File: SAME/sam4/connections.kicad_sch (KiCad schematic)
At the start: 27 parts, among them J11 Conn_01x02_Socket, J13 BM04B-GHS-TBT, J14 BM04B-GHS-TBT, J15 BM04B-GHS-TBT, J16 BM04B-GHS-TBT, J17 BM04B-GHS-TBT, J18 5023860270, J19 BM04B-GHS-TBT, J6 XT60PW-M, J7 XT60PW-M, J8 XT30PW-F, J9 GT-USB-7010ASV, M5 MR30PW-FB

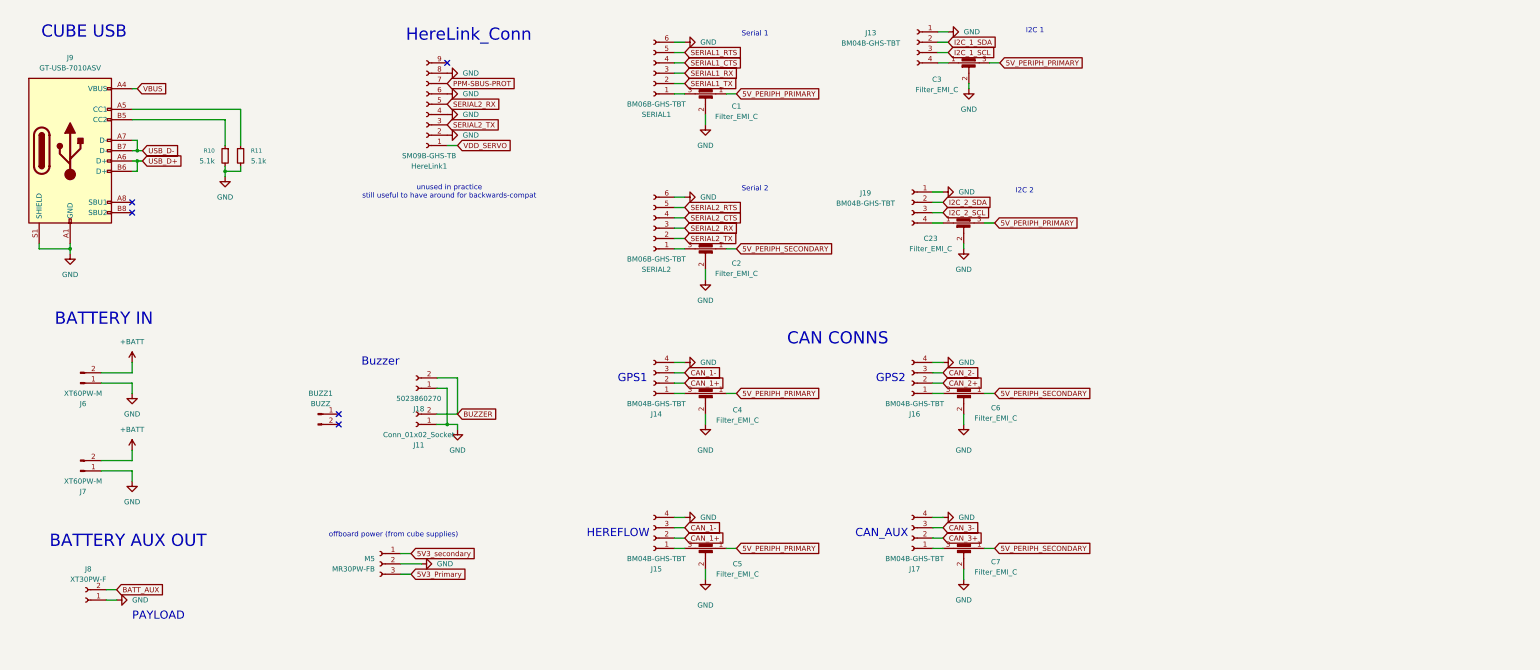
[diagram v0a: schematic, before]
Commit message: final san check routing. add protection
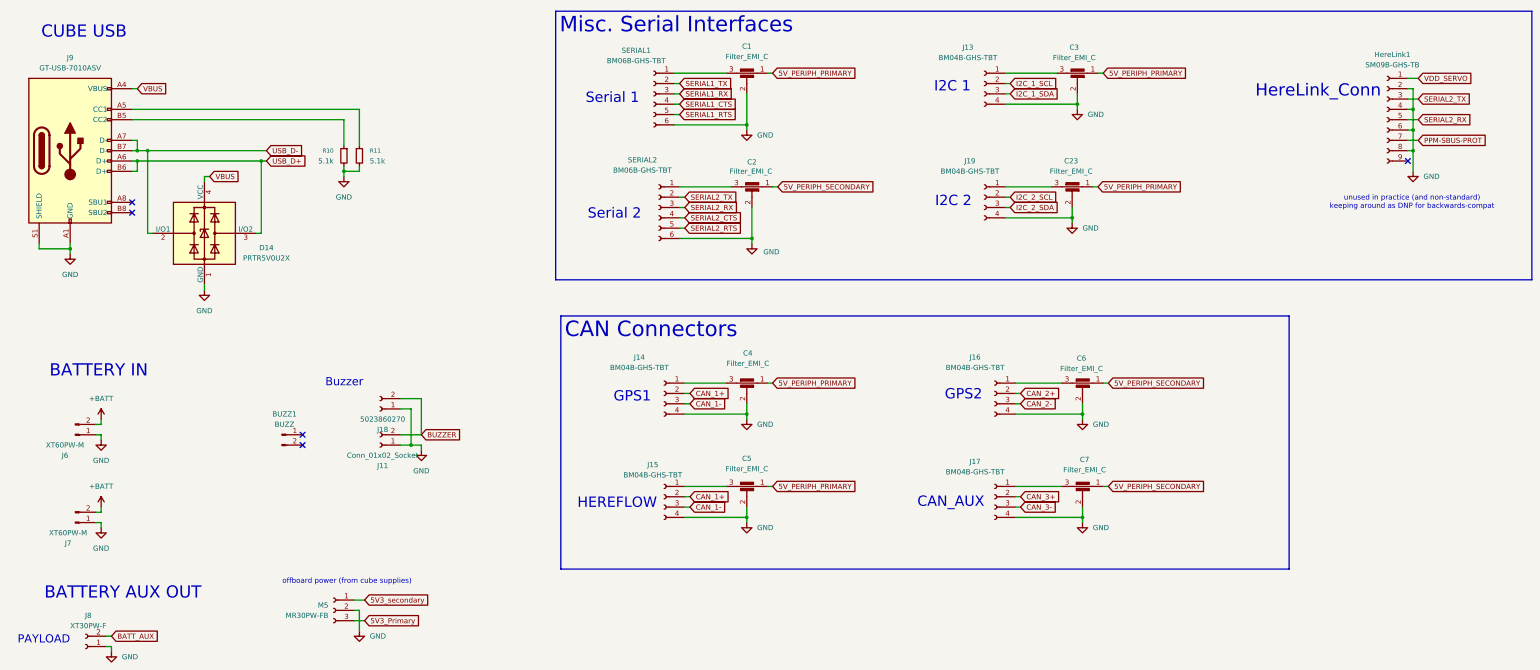
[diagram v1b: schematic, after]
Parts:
- added D14: PRTR5V0U2X, Package_TO_SOT_SMD:SOT-143, symbol Power_Protection:PRTR5V0U2X
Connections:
- net 5V_PERIPH_PRIMARY: now also C23.1, C3.1; no longer C23.3, C3.3
- net GND: now also J13.4 (Pin_4), J19.4 (Pin_4), D14.1 (GND); no longer J13.1 (Pin_1), J19.1 (Pin_1)
- net I2C_1_SCL: now also J13.2 (Pin_2); no longer J13.3 (Pin_3)
- net I2C_1_SDA: now also J13.3 (Pin_3); no longer J13.2 (Pin_2)
- net I2C_2_SCL: now also J19.2 (Pin_2); no longer J19.3 (Pin_3)
- net I2C_2_SDA: now also J19.3 (Pin_3); no longer J19.2 (Pin_2)
- net USB_D+: now also D14.3 (I/O2)
- net USB_D-: now also D14.2 (I/O1)
- net VBUS: now also D14.4 (VCC)
- new net: C23.3, J19.1 (Pin_1)
- new net: C3.3, J13.1 (Pin_1)
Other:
- note added: "unused in practice (and non-standard) keeping around as DNP for backwards-compat"
- note removed: "CAN CONNS"
- note removed: "unused in practice still useful to have around for backwards-compat"
- moved on the sheet: BUZZ1, C1, C2, C23, C3, C4, C5, C6, C7, HereLink1, J11, J13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

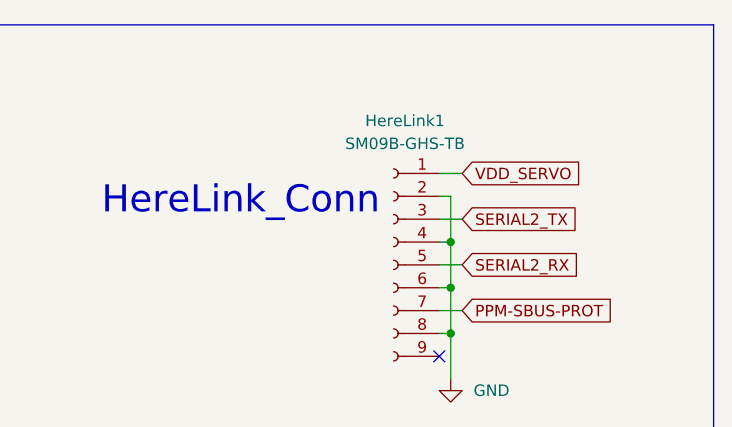
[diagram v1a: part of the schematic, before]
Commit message: update SAME connectors to better fit SAME mechanical design
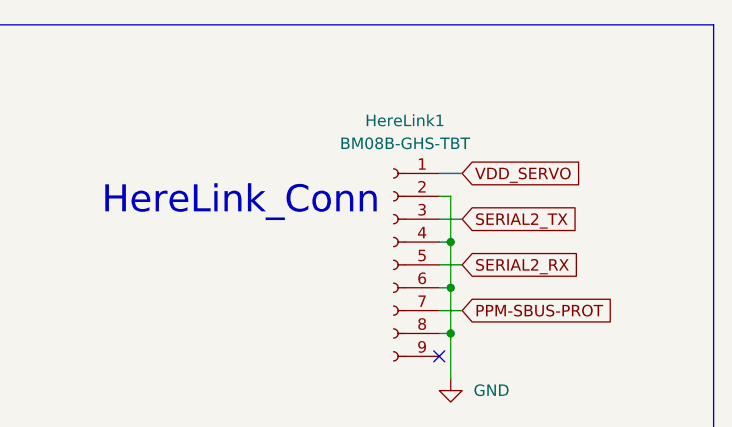
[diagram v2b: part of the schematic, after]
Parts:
- HereLink1: value SM09B-GHS-TB -> BM08B-GHS-TBT; footprint Connector_JST:JST_GH_SM09B-GHS-TB_1x09-1MP_P1.25mm_Horizontal -> Connector_JST:JST_GH_BM08B-GHS-TBT_1x08-1MP_P1.25mm_Vertical; LCSC C265420 -> C133062
